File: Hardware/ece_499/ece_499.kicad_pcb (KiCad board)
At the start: 2 copper layers, 110.8 x 70 mm, 64 parts, among them J1 Conn_01x04, J2 Conn_01x04, J3 Conn_01x04, J4 Conn_01x04, J5 Conn_01x04, Q1 DMN2004WK, Q2 DMN2004WK, Q3 DMN2004WK, Q4 DMN2004WK, SW1 Encoder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

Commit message: fix resistor values, update datasheet
-Fixed R1 values for debounce circuits
-Changed all 2.7k resistors to 3k
-Updated datasheet for DMN2004WK
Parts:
- R11, R13, R14, R15, R16, R3, R5: value 2.7k -> 3k

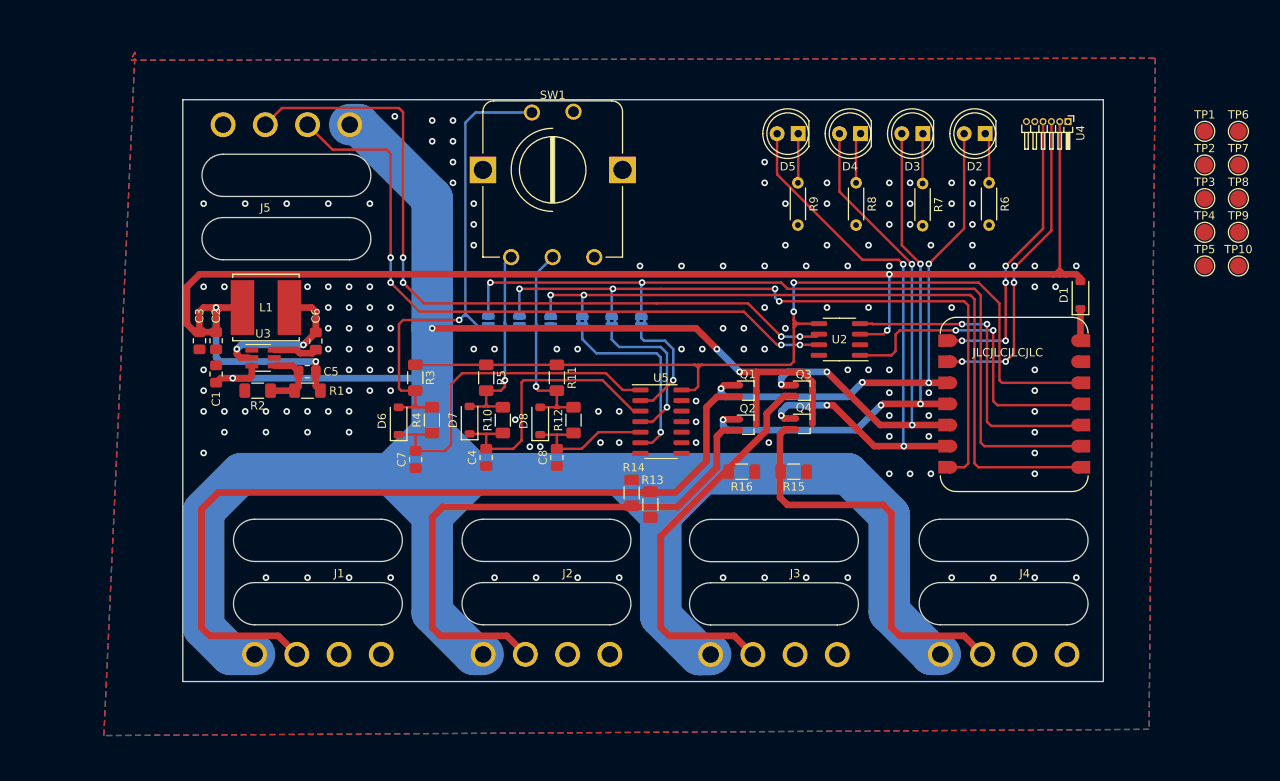
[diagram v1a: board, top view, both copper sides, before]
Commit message: Moved testpoints
-Moved the testpoints onto the board. All are on the front side of the board.
-The zone boundaries are now an actual square.
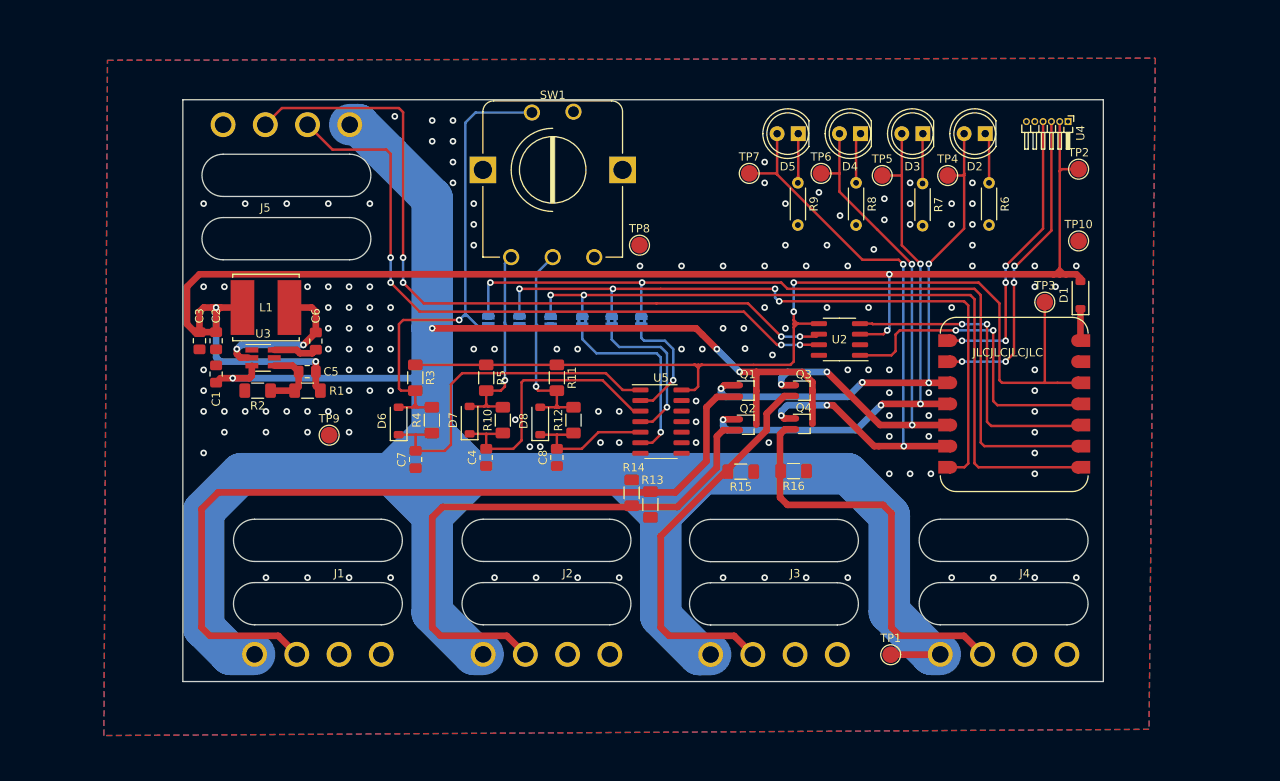
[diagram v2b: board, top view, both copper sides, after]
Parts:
- moved TP9 112.1 mm to (117.6, 70.4)
- moved TP1 73.4 mm to (185.2, 96.8)
- moved TP8 72.3 mm to (154.9, 47.5)
- moved TP7 58.9 mm to (168.1, 38.9)
- moved TP6 50.5 mm to (176.8, 38.9)
- moved TP5 40.3 mm to (184.2, 39.1)
- moved TP4 31.7 mm to (192.0, 39.1)
- moved TP3 22.9 mm to (203.7, 54.4)
- moved TP10 19.5 mm to (207.8, 47.0)
- moved TP2 15.2 mm to (207.8, 38.4)
- moved R15 6.37 mm to (167.1, 74.8)
- moved R16 6.23 mm to (173.5, 74.7)
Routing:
- net +3V3: track 111.0 -> 120.7 mm
- net +12V: track 356.4 -> 362.2 mm
- net valve_4: track 70.9 -> 74.3 mm
- net +5V: track 182.0 -> 184.4 mm
- net valve_2: track 64.4 -> 66.7 mm
- net valve_1: track 62.5 -> 64.8 mm
- net valve_3: track 63.8 -> 66.0 mm
- net GND: vias 148 -> 144

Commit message: Minor fixes     - Replace MCU diode with 1N5817     - Move 3v3 TP     - Remove 90 degree traces     - More stitching vias
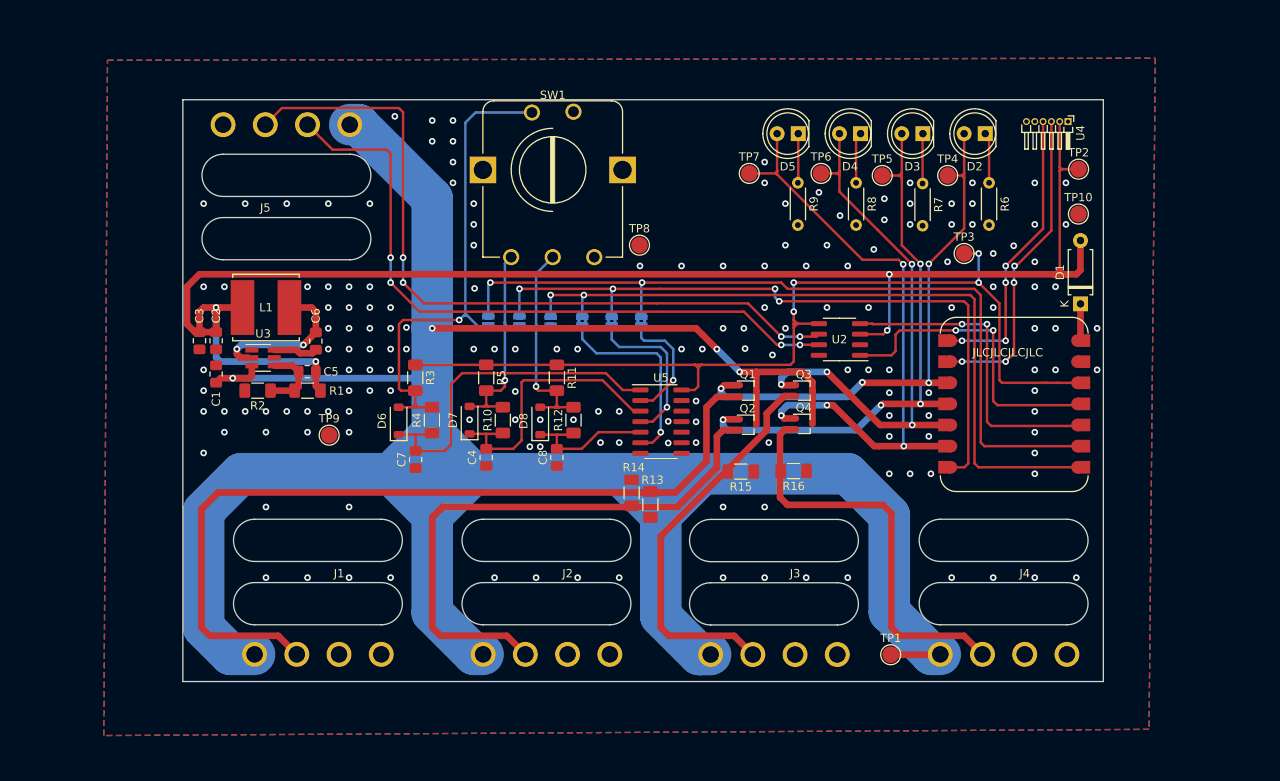
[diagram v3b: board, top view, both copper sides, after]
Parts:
- D1: value B5817W -> 1N5817; footprint Diode_SMD:D_SOD-123 -> Diode_THT:D_A-405_P7.62mm_Horizontal
- moved TP3 11.3 mm to (194.0, 48.5)
- moved TP10 3.24 mm to (207.8, 43.8)
- moved D1 1.06 mm to (208.0, 54.6)
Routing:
- net +3V3: track 120.7 -> 116.3 mm, vias 2 -> 4
- net +5V: track 184.4 -> 188.0 mm
- net valve_2: track 66.7 -> 67.6 mm
- net valve_3: track 66.0 -> 66.8 mm
- net Net-(D1-K): track 4.00 -> 4.59 mm
- net GND: vias 144 -> 169

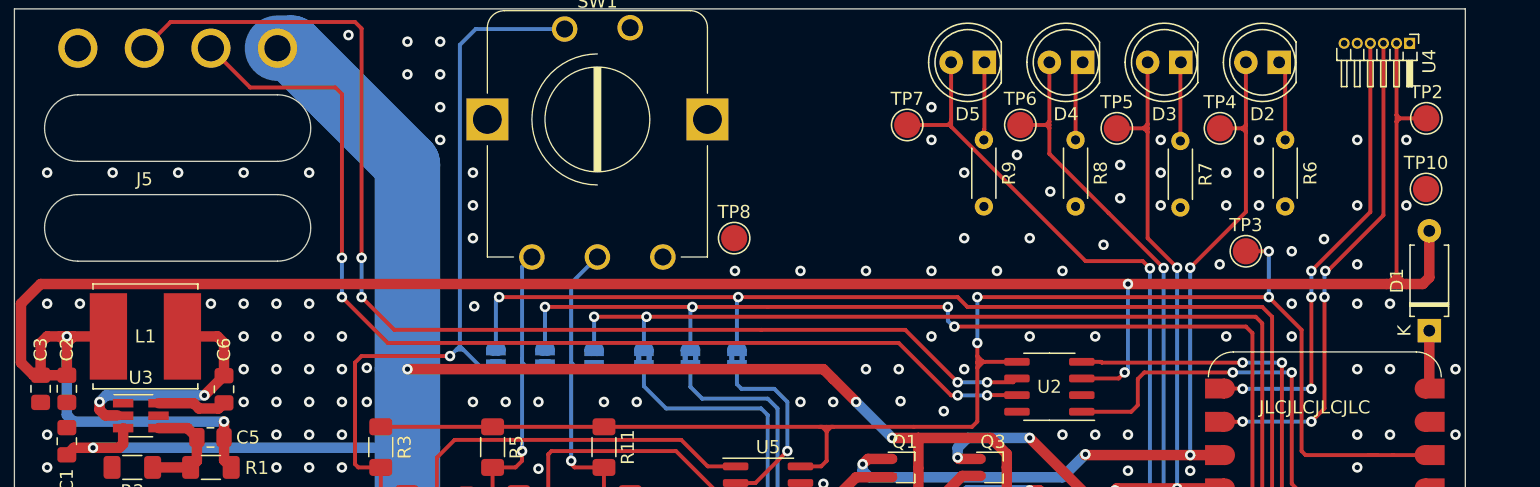
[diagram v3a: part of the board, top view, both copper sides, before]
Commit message: Run DRC     - Validate footprints     - Add thermal trace to reg     - Move TP2 and TP10 to avoid overlapping silk     - More stitching vias :)
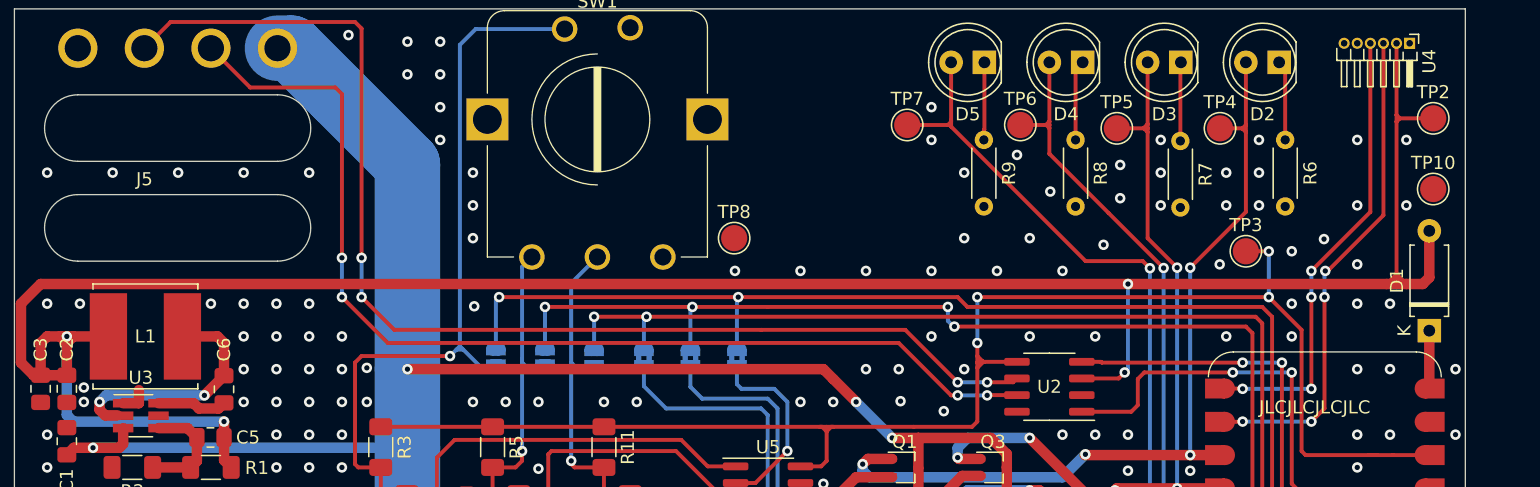
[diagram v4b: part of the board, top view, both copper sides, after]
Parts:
- moved TP10 0.55 mm to (208.3, 43.8)
- moved TP2 0.53 mm to (208.3, 38.4)
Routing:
- net GND: track 0.00 -> 2.20 mm, vias 169 -> 171

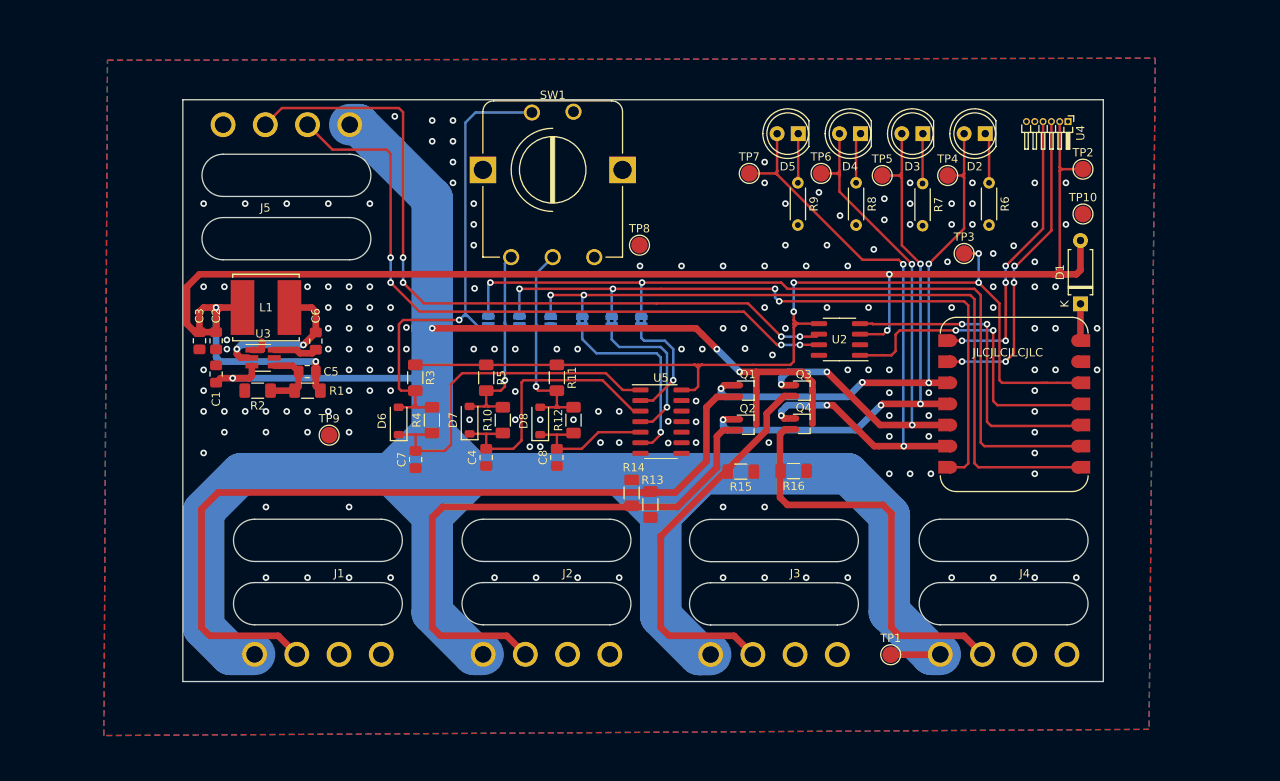
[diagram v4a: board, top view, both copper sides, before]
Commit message: More vias, 3D models
  - More stitching vias
  - Add model for L1
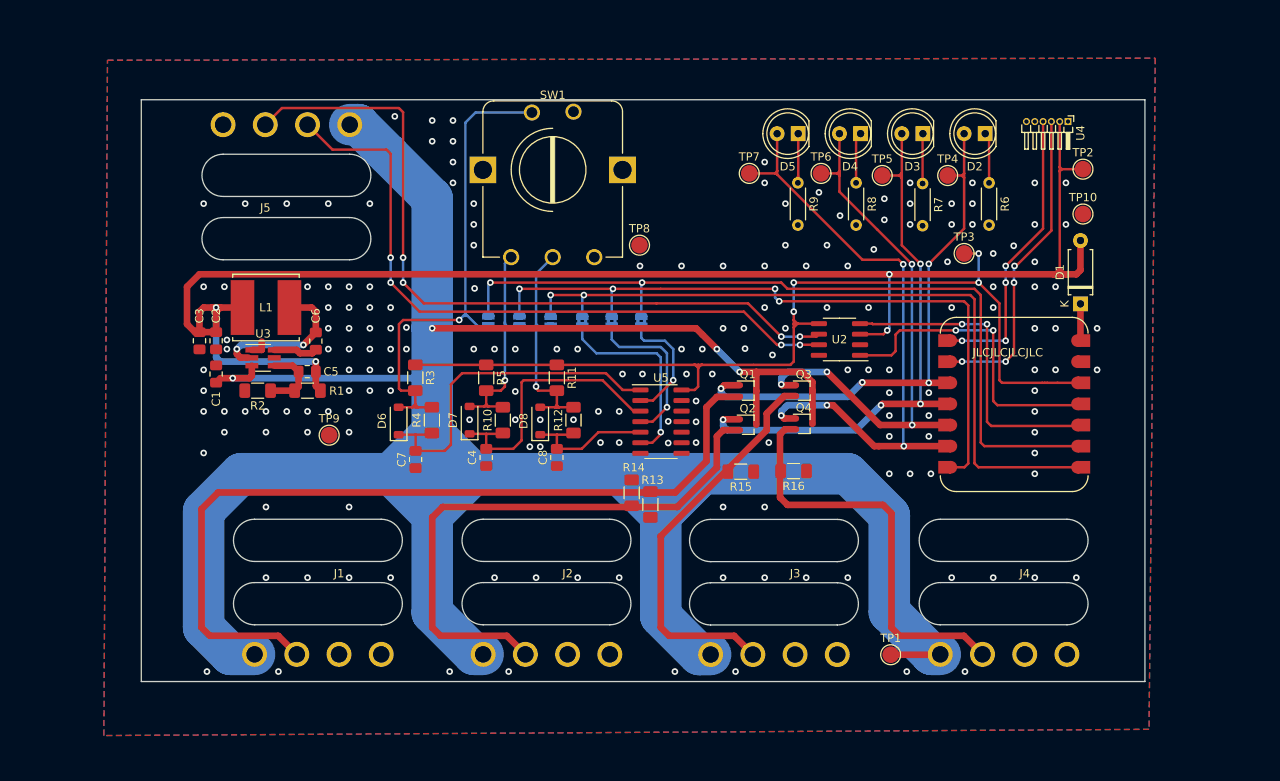
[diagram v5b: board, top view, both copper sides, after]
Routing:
- net GND: vias 171 -> 183
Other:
- board size 110.8 x 70 mm -> 120.8 x 70 mm
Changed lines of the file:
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@@
 			(solder_mask_margin 0.102)
 		)
+		(model "${KIPRJMOD}/Addons/Imported_Parts.pretty/SRN8040TA-6R8M--3DModel-STEP-56544.STEP"
+			(offset
+				(xyz 0 0 0)
+			)
+			(scale
+				(xyz 1 1 1)
+			)
+			(rotate
+				(xyz -90 0 0)
+			)
+		)
 	)
 	(footprint "Resistor_SMD:R_1206_3216Metric_Pad1.30x1.75mm_HandSolder"
@@
 	)
 	(gr_rect
-		(start 100 30)
-		(end 210.75 100)
+		(start 95 30)
+		(end 215.75 100)
 		(stroke
 			(width 0.1)
@@
 	)
 	(via
+		(at 194.1 98.8)
+		(size 0.8)
+		(drill 0.4)
+		(layers "F.Cu" "B.Cu")
+		(free yes)
+		(net 2)
+	)
+	(via
 		(at 102.5 72.5)
 		(size 0.8)
@@
 	)
 	(via
+		(at 166.5 98.8)
+		(size 0.8)
+		(drill 0.4)
+		(layers "F.Cu" "B.Cu")
+		(free yes)
+		(net 2)
+	)
+	(via
 		(at 122.5 62.5)
 		(size 0.8)
@@
 	)
 	(via
+		(at 152.9 63)
+		(size 0.8)
+		(drill 0.4)
+		(layers "F.Cu" "B.Cu")
+		(free yes)
+		(net 2)
+	)
+	(via
 		(at 134.5 68.5)
 		(size 0.8)
@@
 	)
 	(via
+		(at 187.1 98.8)
+		(size 0.8)
+		(drill 0.4)
+		(layers "F.Cu" "B.Cu")
+		(free yes)
+		(net 2)
+	)
+	(via
 		(at 125 60)
 		(size 0.8)
@@
 	)
 	(via
+		(at 139.2 98.8)
+		(size 0.8)
+		(drill 0.4)
+		(layers "F.Cu" "B.Cu")
+		(free yes)
+		(net 2)
+	)
+	(via
 		(at 120 67.5)
 		(size 0.8)
@@
 	)
 	(via
+		(at 155.3 63)
+		(size 0.8)
+		(drill 0.4)
+		(layers "F.Cu" "B.Cu")
+		(free yes)
+		(net 2)
+	)
+	(via
 		(at 197.5 87.5)
 		(size 0.8)
@@
 	)
 	(via
+		(at 159.2 98.8)
+		(size 0.8)
+		(drill 0.4)
+		(layers "F.Cu" "B.Cu")
+		(free yes)
+		(net 2)
+	)
+	(via
 		(at 162.5 60)
 		(size 0.8)
@@
 	)
 	(via
+		(at 132.1 98.8)
+		(size 0.8)
+		(drill 0.4)
+		(layers "F.Cu" "B.Cu")
+		(free yes)
+		(net 2)
+	)
+	(via
 		(at 161.75 66.25)
 		(size 0.8)
@@
 	)
 	(via
+		(at 102.9 98.8)
+		(size 0.8)
+		(drill 0.4)
+		(layers "F.Cu" "B.Cu")
+		(free yes)
+		(net 2)
+	)
+	(via
 		(at 140 68.5)
 		(size 0.8)
@@
 	)
 	(via
+		(at 111.5 98.8)
+		(size 0.8)
+		(drill 0.4)
+		(layers "F.Cu" "B.Cu")
+		(free yes)
+		(net 2)
+	)
+	(via
 		(at 102.5 52.5)
 		(size 0.8)
@@
 	)
 	(via
+		(at 163.7 63)
+		(size 0.8)
+		(drill 0.4)
+		(layers "F.Cu" "B.Cu")
+		(free yes)
+		(net 2)
+	)
+	(via
 		(at 202.5 49.5)
 		(size 0.8)
@@
 		(size 0.8)
 		(drill 0.4)
+		(layers "F.Cu" "B.Cu")
+		(free yes)
+		(net 2)
+	)
+	(via
+		(at 160.6 63)
+		(size 0.8)
+		(drill 0.4)

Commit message: Mounting points     - Add M3 mounting points     - Clean up board edges     - Validate manufacturing clearances
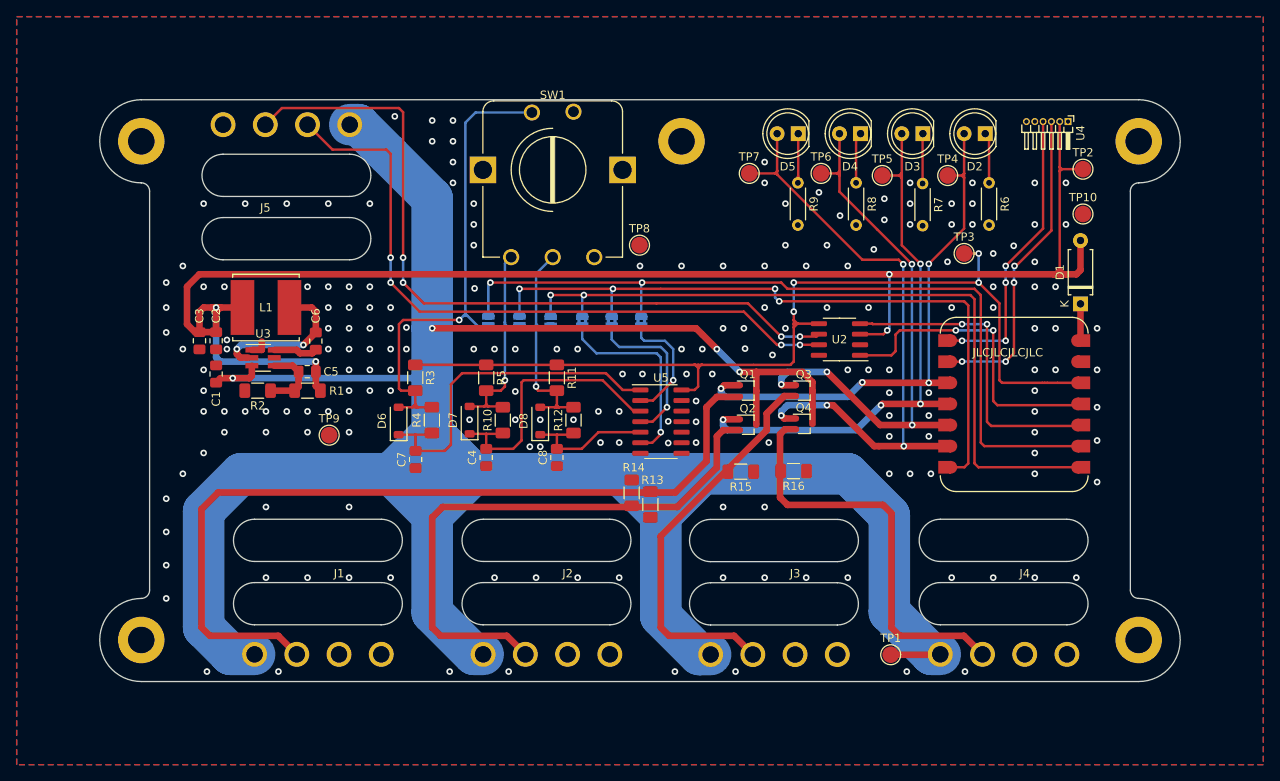
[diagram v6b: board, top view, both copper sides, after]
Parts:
- added REF**: MountingHole_3.2mm_M3_DIN965_Pad, MountingHole:MountingHole_3.2mm_M3_DIN965_Pad, F.Cu at (215.0, 35.0)
- added REF**: MountingHole_3.2mm_M3_DIN965_Pad, MountingHole:MountingHole_3.2mm_M3_DIN965_Pad, F.Cu at (95.0, 35.0)
- added REF**: MountingHole_3.2mm_M3_DIN965_Pad, MountingHole:MountingHole_3.2mm_M3_DIN965_Pad, F.Cu at (95.0, 95.0)
- added REF**: MountingHole_3.2mm_M3_DIN965_Pad, MountingHole:MountingHole_3.2mm_M3_DIN965_Pad, F.Cu at (215.0, 95.0)
- added REF**: MountingHole_3.2mm_M3_DIN965_Pad, MountingHole:MountingHole_3.2mm_M3_DIN965_Pad, F.Cu at (160.0, 35.0)
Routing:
- net GND: vias 183 -> 196
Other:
- board size 120.8 x 70 mm -> 130 x 70 mm
